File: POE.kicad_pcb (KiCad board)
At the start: 2 copper layers, 40 x 70 mm, 17 parts, among them J1 Conn_01x02_Male

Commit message: Some layout rework...
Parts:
- moved J1 21.1 mm to (106.0, 85.7), turned to 0 degrees
- moved R3 13.0 mm to (116.5, 74.0), turned to 180 degrees
- moved C2 10.0 mm to (93.0, 83.0)
- moved C1 9.37 mm to (100.0, 85.0), turned to 180 degrees
- moved TR3 2.68 mm to (105.1, 123.0)
- moved R1 1.12 mm to (116.5, 78.0), turned to 180 degrees
- moved R2 1.12 mm to (116.5, 80.0), turned to 0 degrees
- moved D1 1.00 mm to (87.0, 74.0)
- moved D2 1.00 mm to (87.0, 82.0)
- moved G*** 1.00 mm to (82.0, 110.2)
- moved REF** 1.00 mm to (118.0, 132.0)
- moved REF** 1.00 mm to (82.0, 132.0)
- moved REF** 1.00 mm to (82.4, 89.0)
- moved REF** 1.00 mm to (118.0, 68.0)
- moved REF** 1.00 mm to (82.0, 68.0)
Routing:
- net VA1: track 46.2 -> 51.0 mm
- net VB1: track 53.3 -> 57.8 mm
- net VB2: track 51.4 -> 55.8 mm
- net VA2: track 40.3 -> 44.4 mm
- net Net-(RJ1-Pad7): track 15.9 -> 13.8 mm
- net Net-(RJ1-Pad6): track 19.8 -> 18.3 mm
- net Net-(RJ1-Pad1): track 27.2 -> 28.6 mm
- net Net-(RJ1-Pad5): track 22.2 -> 23.5 mm
- net Vin-: track 19.0 -> 20.0 mm
- net Vin+: track 32.6 -> 33.5 mm
- net Net-(RJ1-Pad3): track 17.5 -> 18.3 mm
- net Net-(RJ1-Pad2): track 29.0 -> 29.7 mm
- net Net-(RJ1-Pad8): track 15.2 -> 14.6 mm
- net ADJ: track 6.27 -> 5.76 mm
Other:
- board size 40 x 70 mm -> 42 x 70 mm

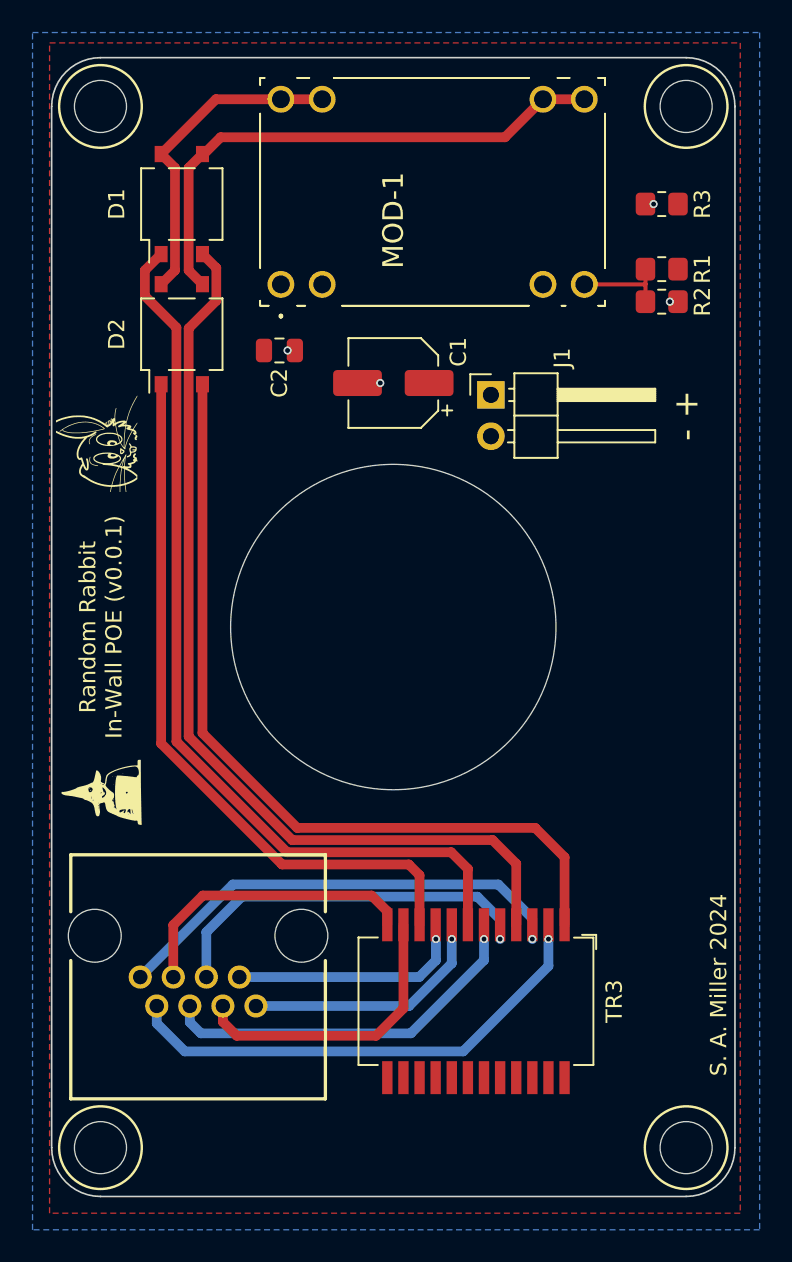
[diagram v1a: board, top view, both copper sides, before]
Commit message: Improved Vout filtering
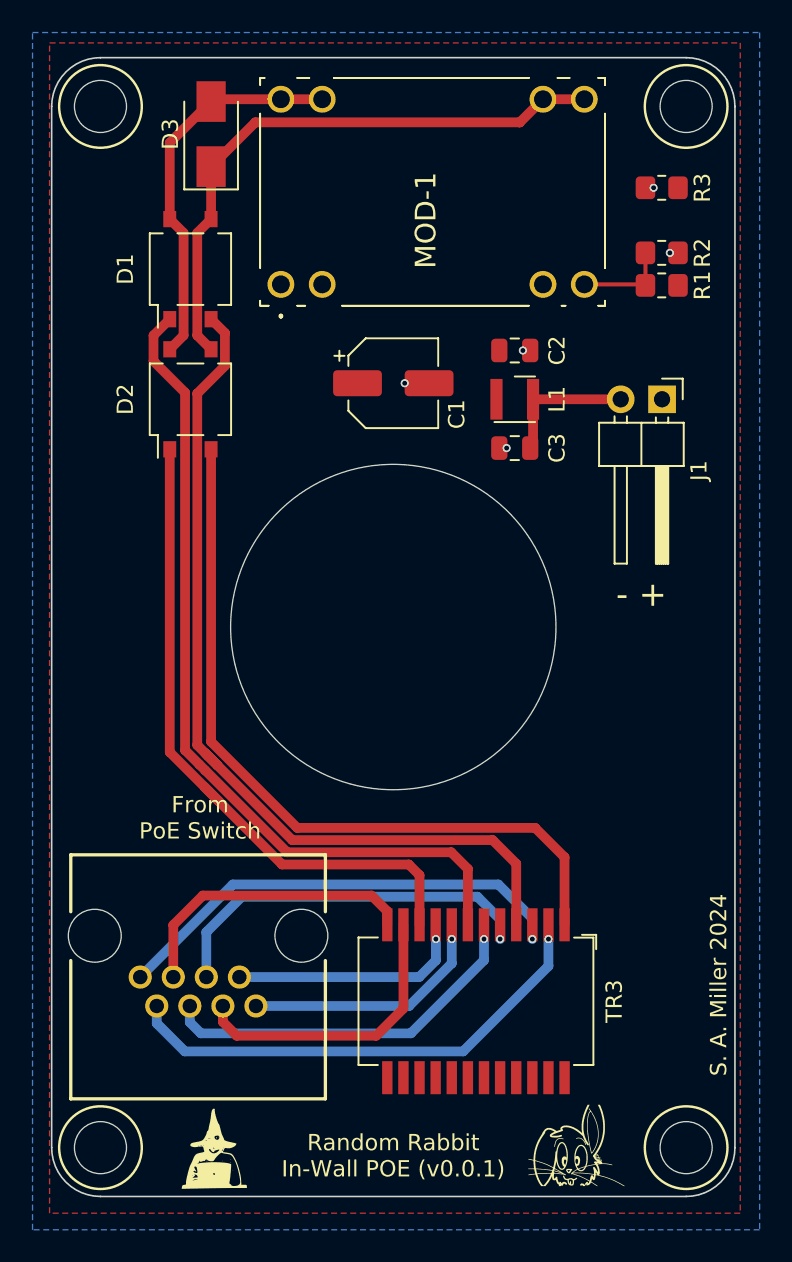
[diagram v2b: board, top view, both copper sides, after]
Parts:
- added C3: 10uf, Capacitor_SMD:C_0805_2012Metric, F.Cu at (107.5, 89.0)
- added D3: SMAJ58A, Diode_SMD:D_SMA, F.Cu at (88.8, 69.7)
- added L1: fnr3015s1r, tightstuff:fnr3015s, F.Cu at (107.5, 86.0)
- moved REF** 52.1 mm to (111.0, 132.5), turned to 0 degrees
- moved G*** 22.9 mm to (89.0, 132.0), turned to 0 degrees
- moved C2 14.5 mm to (107.5, 83.0)
- moved J1 10.5 mm to (116.5, 86.0), turned to -90 degrees
- moved D1 4.03 mm to (87.5, 78.0)
- moved D2 4.03 mm to (87.5, 86.0)
- moved R2 3.00 mm to (116.5, 77.0)
- moved R1 1.00 mm to (116.5, 79.0)
- moved R3 1.00 mm to (116.5, 73.0)
- turned C1 to 0 degrees
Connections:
- J1 pad 1: Vout -> GND
- J1 pad 2: GND -> VoutF
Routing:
- net VoutF: track 0.00 -> 8.46 mm
- net VB2: track 55.8 -> 51.6 mm
- net VA1: track 51.0 -> 46.8 mm
- net Vin-: track 20.0 -> 23.9 mm
- net VB1: track 57.8 -> 54.7 mm
- net Vin+: track 33.5 -> 36.6 mm
- net VA2: track 44.4 -> 41.4 mm
- net GND: vias 4 -> 5
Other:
- board text added: "Ag9900 datasheet Figure 13 ?"
- board text added: "From PoE Switch"

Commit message: ...
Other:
- board text added: "+ -"
- board text removed: "- +"
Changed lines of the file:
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@@
     (effects (font (size 1 1) (thickness 0.15)))
   )
-  (gr_text "- +" (at 115.250055 98) (layer "F.SilkS")
+  (gr_text "+ -" (at 115.250055 98) (layer "F.SilkS")
     (effects (font (size 1.5 1.5) (thickness 0.25)))
   )

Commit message: foorprint improvements & parts selections...
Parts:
- C1: footprint Capacitor_SMD:CP_Elec_5x3 -> Capacitor_SMD:CP_Elec_6.3x5.4
- TR3: value TG111-MSC13LF -> SET2401ST; footprint Transformer_SMD:Transformer_Ethernet_HALO_TG111-MSC13 -> tightstuff:Eth_Magnetics (1.0)
- moved C1 0.99 mm to (100.0, 86.0), turned to 180 degrees
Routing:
- net Net-(RJ1-Pad2): track 29.7 -> 29.1 mm

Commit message: Prepping for possible first build...
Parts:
- added D4: LED, LED_SMD:LED_0805_2012Metric, F.Cu at (116.5, 122.0)
- added R4: ?, Resistor_SMD:R_0805_2012Metric_Pad1.20x1.40mm_HandSolder, F.Cu at (116.5, 124.0)
- renumbered RJ1 to J1, J1 to J2
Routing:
- net Net-(D4-Pad2): track 0.00 -> 2.03 mm
- net GND: vias 5 -> 6

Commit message: gerbers produced, boards & parts ordered... (w/slow-boat shipping...)
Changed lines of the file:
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@@
     (grid_origin 100 100)
     (pcbplotparams
-      (layerselection 0x0000030_7ffffffe)
+      (layerselection 0x00010ff_ffffffff)
       (disableapertmacros false)
       (usegerberextensions false)
@@
       (sketchpadsonfab false)
       (subtractmaskfromsilk false)
-      (outputformat 3)
+      (outputformat 1)
       (mirror false)
       (drillshape 0)
       (scaleselection 1)
-      (outputdirectory "3D/")
+      (outputdirectory "Gerbers/")
     )
   )
@@
     (fp_line (start 1 -0.625) (end 1 0.625) (layer "F.Fab") (width 0.1))
     (fp_line (start -1 0.625) (end -1 -0.625) (layer "F.Fab") (width 0.1))
-    (pad "1" smd roundrect (at -1 0) (size 1.2 1.4) (layers "F.Cu" "F.Paste" "F.Mask") (roundrect_rratio 0.208333)
+    (pad "1" smd roundrect (at -1 0) (size 1.2 1.4) (layers "F.Cu" "F.Paste" "F.Mask") (roundrect_rratio 0.2083333333)
       (net 1 "Vout") (pintype "passive"))
-    (pad "2" smd roundrect (at 1 0) (size 1.2 1.4) (layers "F.Cu" "F.Paste" "F.Mask") (roundrect_rratio 0.208333)
+    (pad "2" smd roundrect (at 1 0) (size 1.2 1.4) (layers "F.Cu" "F.Paste" "F.Mask") (roundrect_rratio 0.2083333333)
       (net 23 "Net-(D4-Pad2)") (pintype "passive"))
     (model "${KICAD6_3DMODEL_DIR}/Resistor_SMD.3dshapes/R_0805_2012Metric.wrl"
@@
     (fp_line (start -1 0.625) (end -1 -0.625) (layer "F.Fab") (width 0.1))
     (fp_line (start 1 0.625) (end -1 0.625) (layer "F.Fab") (width 0.1))
-    (pad "1" smd roundrect (at -1 0 180) (size 1.2 1.4) (layers "F.Cu" "F.Paste" "F.Mask") (roundrect_rratio 0.208333)
+    (pad "1" smd roundrect (at -1 0 180) (size 1.2 1.4) (layers "F.Cu" "F.Paste" "F.Mask") (roundrect_rratio 0.2083333333)
       (net 1 "Vout") (pintype "passive"))
-    (pad "2" smd roundrect (at 1 0 180) (size 1.2 1.4) (layers "F.Cu" "F.Paste" "F.Mask") (roundrect_rratio 0.208333)
+    (pad "2" smd roundrect (at 1 0 180) (size 1.2 1.4) (layers "F.Cu" "F.Paste" "F.Mask") (roundrect_rratio 0.2083333333)
       (net 2 "GND") (pintype "passive"))
     (model "${KICAD6_3DMODEL_DIR}/Resistor_SMD.3dshapes/R_0805_2012Metric.wrl"
@@
     (fp_line (start -1 0.625) (end -1 -0.625) (layer "F.Fab") (width 0.1))
     (fp_line (start 1 0.625) (end -1 0.625) (layer "F.Fab") (width 0.1))
-    (pad "1" smd roundrect (at -1 0 180) (size 1.2 1.4) (layers "F.Cu" "F.Paste" "F.Mask") (roundrect_rratio 0.208333)
+    (pad "1" smd roundrect (at -1 0 180) (size 1.2 1.4) (layers "F.Cu" "F.Paste" "F.Mask") (roundrect_rratio 0.2083333333)
       (net 1 "Vout") (pintype "passive"))
-    (pad "2" smd roundrect (at 1 0 180) (size 1.2 1.4) (layers "F.Cu" "F.Paste" "F.Mask") (roundrect_rratio 0.208333)
+    (pad "2" smd roundrect (at 1 0 180) (size 1.2 1.4) (layers "F.Cu" "F.Paste" "F.Mask") (roundrect_rratio 0.2083333333)
       (net 3 "ADJ") (pintype "passive"))
     (model "${KICAD6_3DMODEL_DIR}/Resistor_SMD.3dshapes/R_0805_2012Metric.wrl"
@@
     (fp_line (start -1 0.625) (end -1 -0.625) (layer "F.Fab") (width 0.1))
     (fp_line (start 1 -0.625) (end 1 0.625) (layer "F.Fab") (width 0.1))
-    (pad "1" smd roundrect (at -1 0) (size 1.2 1.4) (layers "F.Cu" "F.Paste" "F.Mask") (roundrect_rratio 0.208333)
+    (pad "1" smd roundrect (at -1 0) (size 1.2 1.4) (layers "F.Cu" "F.Paste" "F.Mask") (roundrect_rratio 0.2083333333)
       (net 3 "ADJ") (pintype "passive"))
-    (pad "2" smd roundrect (at 1 0) (size 1.2 1.4) (layers "F.Cu" "F.Paste" "F.Mask") (roundrect_rratio 0.208333)
+    (pad "2" smd roundrect (at 1 0) (size 1.2 1.4) (layers "F.Cu" "F.Paste" "F.Mask") (roundrect_rratio 0.2083333333)
       (net 2 "GND") (pintype "passive"))
     (model "${KICAD6_3DMODEL_DIR}/Resistor_SMD.3dshapes/R_0805_2012Metric.wrl"
